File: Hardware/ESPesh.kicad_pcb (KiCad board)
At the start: 2 copper layers, 25.4 x 25.4 mm, 38 parts, among them IC1 ESP32-PICO-D4, IC3 FDN340P, U1 SPX3819M5-L-3-3, U2 SL4054ST25P, U3 XB6566H0, U4 HDC1080

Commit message: rev0.3 and panelized gerbers
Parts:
- added 3V3: Conn_01x01, CustomFootprints:RoundPadPassthrough, F.Cu at (144.4, 88.3)
- added GND: Conn_01x01, CustomFootprints:RoundPadPassthrough, F.Cu at (161.2, 105.7)
- added GND: Conn_01x01, CustomFootprints:RoundPadPassthrough, F.Cu at (141.6, 93.0)
- 3V3: renamed from GND; footprint CustomFootprints:RoundPad -> CustomFootprints:RoundPadPassthrough
- D18, D21, D22, D25: footprint CustomFootprints:RoundPad -> CustomFootprints:RoundPadPassthrough
- RXD: renamed from D19; footprint CustomFootprints:RoundPad -> CustomFootprints:RoundPadPassthrough
- TXD: renamed from D23; footprint CustomFootprints:RoundPad -> CustomFootprints:RoundPadPassthrough
- moved 3V3 1.12 mm to (162.4, 104.4), turned to 320 degrees
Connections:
- 3V3 pad 1: GND -> +3V3
- RXD pad 1: /IO19 -> /RXD
- TXD pad 1: /IO23 -> /TXD
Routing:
- net +3V3: track 56.5 -> 68.2 mm
- net /IO19: track 10.7 -> 0.00 mm, vias 2 -> 0
- net /TXD: track 0.00 -> 9.98 mm, vias 0 -> 2
- net /IO23: track 9.85 -> 0.00 mm, vias 2 -> 0
- net /RXD: track 0.00 -> 9.67 mm, vias 0 -> 2
- net GND: track 30.6 -> 33.2 mm, vias 32 -> 31
- net /IO22: track 10.3 -> 11.5 mm

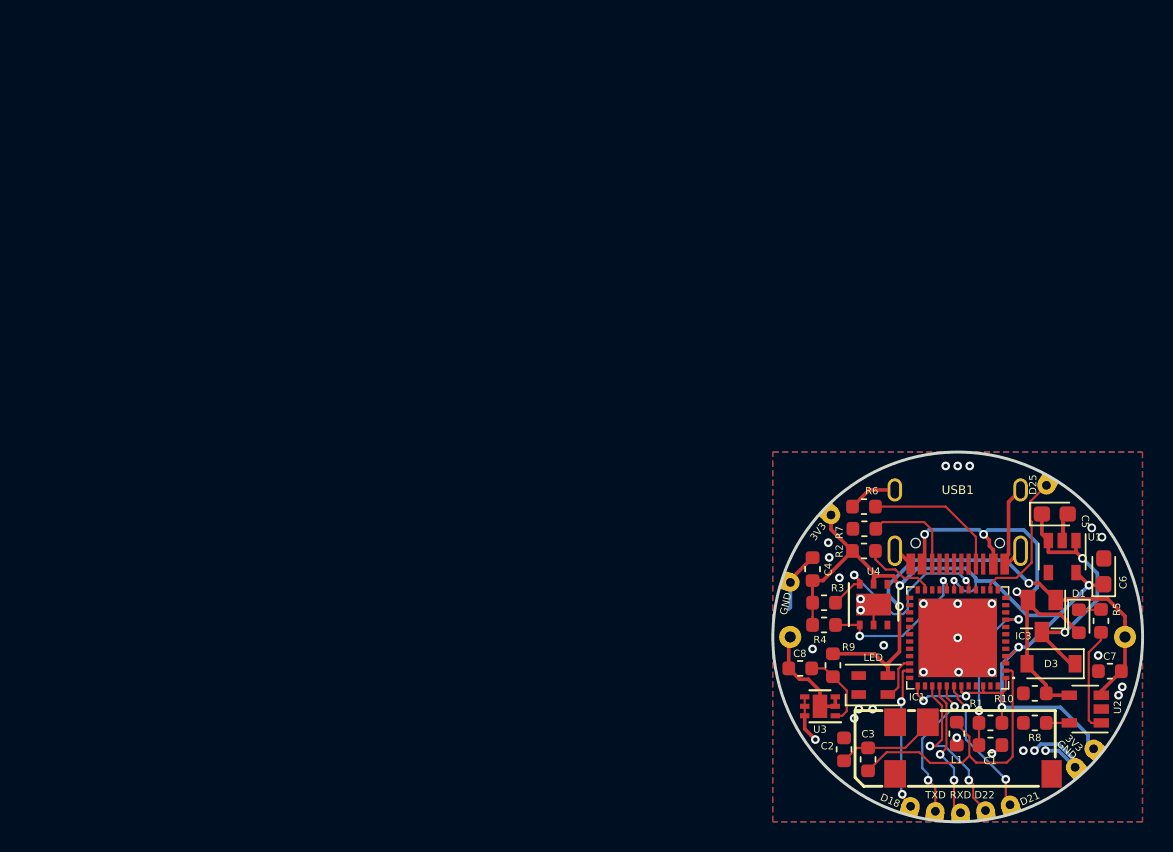
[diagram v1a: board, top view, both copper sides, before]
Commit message: #1 Minor fixes and rev0.3 tested (antenna not tested yet)
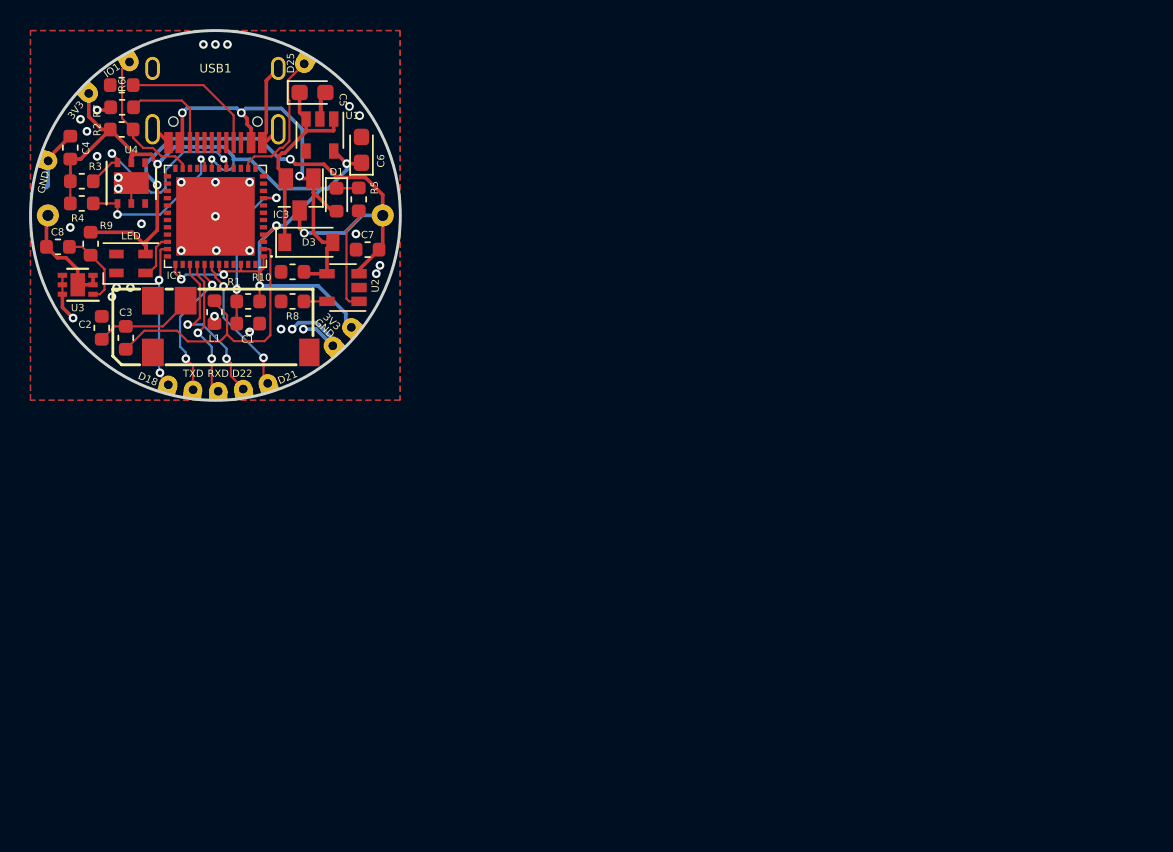
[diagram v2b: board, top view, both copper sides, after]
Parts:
- added IO1: Conn_01x01, CustomFootprints:RoundPadPassthrough, F.Cu at (96.2, 57.2)
- moved ANT1 58.6 mm to (95.1, 75.4)
- moved C2 58.6 mm to (94.3, 75.5)
- moved C5 58.6 mm to (108.8, 59.3)
- moved D18 58.6 mm to (98.9, 79.4)
- moved GND 58.6 mm to (110.2, 76.7)
- moved IC3 58.6 mm to (107.9, 66.3)
- moved R2 58.6 mm to (95.7, 61.8)
- moved R3 58.6 mm to (92.9, 65.4)
- moved R4 58.6 mm to (92.9, 66.9)
- moved R6 58.6 mm to (95.7, 58.8)
- moved TXD 58.6 mm to (100.6, 79.7)
- moved U2 58.6 mm to (110.9, 72.7)
- moved D25 58.6 mm to (108.2, 57.3)
- moved R9 58.6 mm to (93.5, 69.7)
- moved 3V3 58.6 mm to (111.4, 75.4)
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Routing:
- net +BATT: track 36.3 -> 44.0 mm, vias 2 -> 3
- net /IO0: track 5.02 -> 10.2 mm
- net VDD: track 17.4 -> 14.9 mm, vias 2 -> 0
- net GND: track 33.2 -> 30.9 mm, vias 31 -> 32
- net VCC: track 31.8 -> 29.9 mm
